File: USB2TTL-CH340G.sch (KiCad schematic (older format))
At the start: 20 parts, among them P1 PWR, P2 USB_OTG, P3 PWR_SEL, P4 CONN_01X06, U1 CH340G, X1 CRYSTAL_SMD

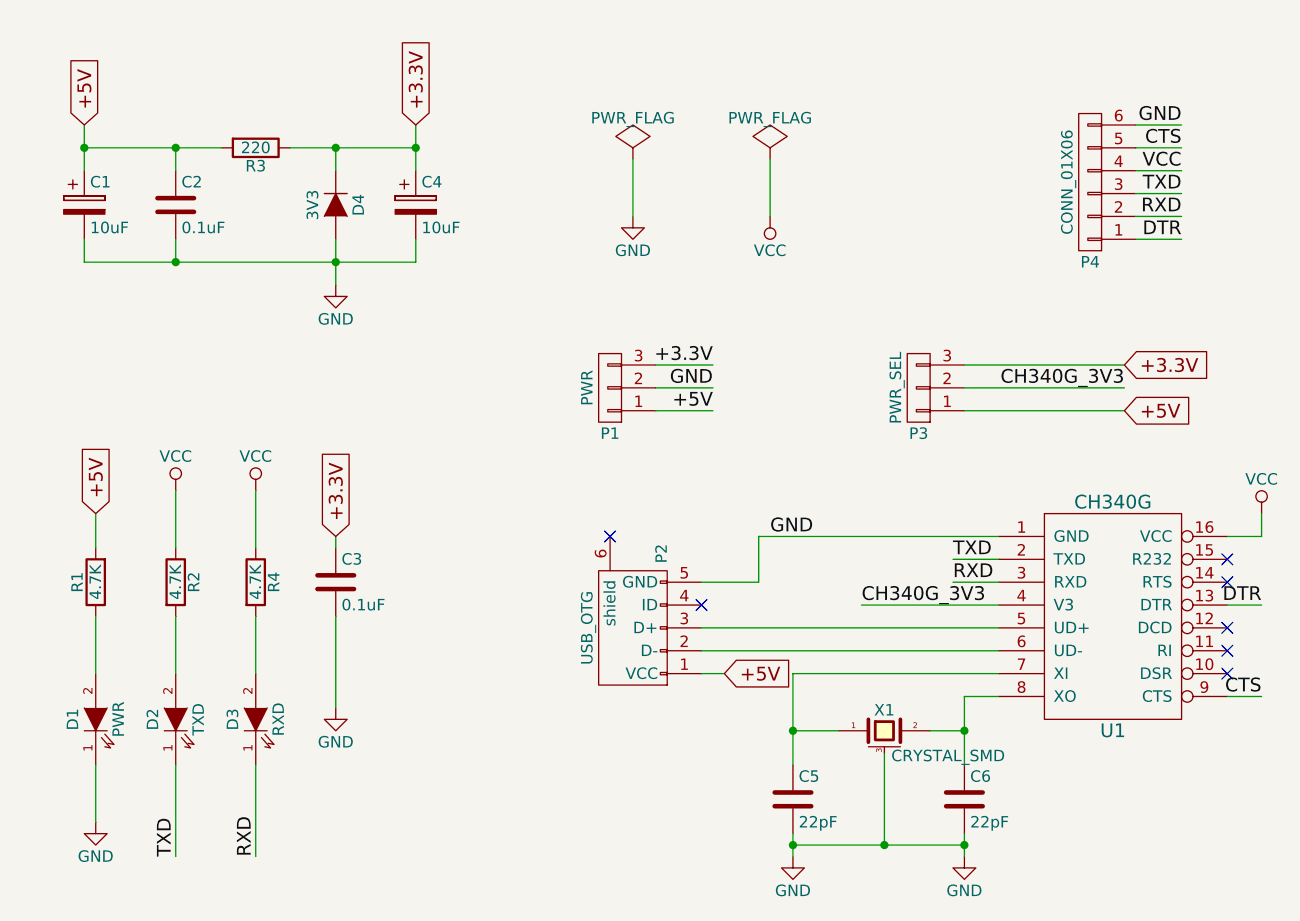
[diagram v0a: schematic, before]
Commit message: 更新为版本v0.2，修改内容如下：1.修复电源电路连接问题（v3和VCC）。2.重新布局使元件更紧凑，板型加入圆角。3.更改USB接口的封装。4.导出最新gerber及drill钻孔文件。
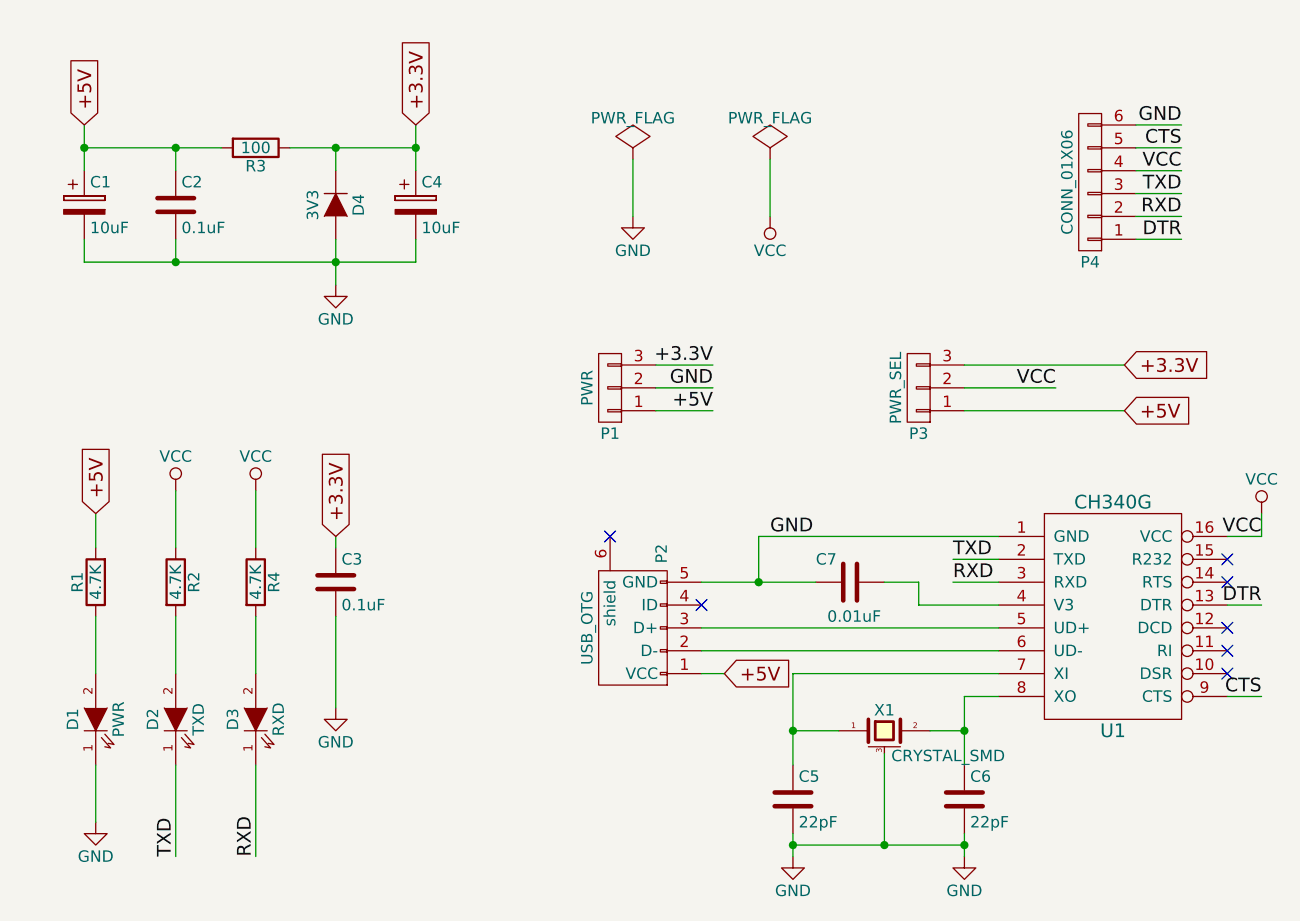
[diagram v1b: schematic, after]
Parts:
- added C7: 0.01uF, Capacitors_SMD:C_0603, symbol C
- C1, C2, C3, C4, C5, C6: footprint Capacitors_SMD:C_0603_HandSoldering -> Capacitors_SMD:C_0603
- P2: footprint Connect:USB_Micro-B -> myFootprints:USB_Micro-B-MK5
- R3: value 220 -> 100
- X1: footprint Crystals:Resonator_3.2x1.5mm -> myFootprints:Resonator_3.2x1.5mm
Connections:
- net GND: now also C7.2
- net VCC: now also P3.2 (P2)
- net CH340G_3V3: no longer names the net of U1.4 (V3)
- net CH340G_3V3: now also C7.1; no longer P3.2 (P2)
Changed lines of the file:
@@
 LIBS:valves
 LIBS:ch340g
+LIBS:USB2TTL-CH340G-cache
 EELAYER 25 0
 EELAYER END
@@
 Title "USB2TTL-CH340G"
 Date "2016-06-03"
-Rev "v0.1"
-Comp ""
-Comment1 ""
+Rev "v0.2"
+Comp "SMSLIT"
+Comment1 "Author: 5km"
 Comment2 ""
 Comment3 ""
@@
 F 0 "C1" H 3325 2950 50  0000 L CNN
 F 1 "10uF" H 3325 2750 50  0000 L CNN
-F 2 "Capacitors_SMD:C_0603_HandSoldering" H 3338 2700 50  0001 C CNN
+F 2 "Capacitors_SMD:C_0603" H 3338 2700 50  0001 C CNN
 F 3 "" H 3300 2850 50  0000 C CNN
 	1    3300 2850
@@
 F 0 "C4" H 4775 2950 50  0000 L CNN
 F 1 "10uF" H 4775 2750 50  0000 L CNN
-F 2 "Capacitors_SMD:C_0603_HandSoldering" H 4788 2700 50  0001 C CNN
+F 2 "Capacitors_SMD:C_0603" H 4788 2700 50  0001 C CNN
 F 3 "" H 4750 2850 50  0000 C CNN
 	1    4750 2850
@@
 F 0 "C2" H 3725 2950 50  0000 L CNN
 F 1 "0.1uF" H 3725 2750 50  0000 L CNN
-F 2 "Capacitors_SMD:C_0603_HandSoldering" H 3738 2700 50  0001 C CNN
+F 2 "Capacitors_SMD:C_0603" H 3738 2700 50  0001 C CNN
 F 3 "" H 3700 2850 50  0000 C CNN
 	1    3700 2850
@@
 P 4050 2600
 F 0 "R3" V 4130 2600 50  0000 C CNN
-F 1 "220" V 4050 2600 50  0000 C CNN
+F 1 "100" V 4050 2600 50  0000 C CNN
 F 2 "Resistors_SMD:R_0603" V 3980 2600 50  0001 C CNN
 F 3 "" H 4050 2600 50  0000 C CNN
@@
 F 0 "C3" H 4425 4600 50  0000 L CNN
 F 1 "0.1uF" H 4425 4400 50  0000 L CNN
-F 2 "Capacitors_SMD:C_0603_HandSoldering" H 4438 4350 50  0001 C CNN
+F 2 "Capacitors_SMD:C_0603" H 4438 4350 50  0001 C CNN
 F 3 "" H 4400 4500 50  0000 C CNN
 	1    4400 4500
@@
 F 0 "C5" H 6425 5550 50  0000 L CNN
 F 1 "22pF" H 6425 5350 50  0000 L CNN
-F 2 "Capacitors_SMD:C_0603_HandSoldering" H 6438 5300 50  0001 C CNN
+F 2 "Capacitors_SMD:C_0603" H 6438 5300 50  0001 C CNN
 F 3 "" H 6400 5450 50  0000 C CNN
 	1    6400 5450
@@
 F 0 "C6" H 7175 5550 50  0000 L CNN
 F 1 "22pF" H 7175 5350 50  0000 L CNN
-F 2 "Capacitors_SMD:C_0603_HandSoldering" H 7188 5300 50  0001 C CNN
+F 2 "Capacitors_SMD:C_0603" H 7188 5300 50  0001 C CNN
 F 3 "" H 7150 5450 50  0000 C CNN
 	1    7150 5450
@@
 NoConn ~ 8300 4800
 NoConn ~ 8300 4900
-Text Label 6700 4600 0    60   ~ 0
-CH340G_3V3
 Text Label 7100 4500 0    60   ~ 0
 RXD
@@
 	-1   0    0    1
 $EndComp
-Text Label 7850 3650 2    60   ~ 0
-CH340G_3V3
 $Comp
 L CRYSTAL_SMD X1
@@
 F 0 "X1" H 6800 5240 50  0000 C CNN
 F 1 "CRYSTAL_SMD" H 6830 5040 50  0000 L CNN
-F 2 "Crystals:Resonator_3.2x1.5mm" H 6800 5150 50  0001 C CNN
+F 2 "myFootprints:Resonator_3.2x1.5mm" H 6800 5150 50  0001 C CNN
 F 3 "" H 6800 5150 50  0000 C CNN
 	1    6800 5150
@@
 F 0 "P2" H 6025 4575 50  0000 C CNN
 F 1 "USB_OTG" H 5700 4900 50  0000 C CNN
-F 2 "Connect:USB_Micro-B" V 5650 4600 50  0001 C CNN
+F 2 "myFootprints:USB_Micro-B-MK5" V 5650 4600 50  0001 C CNN
 F 3 "" V 5650 4600 50  0000 C CNN
 	1    5700 4700
@@
 	6000 4700 7300 4700
 Wire Wire Line
-	6700 4600 7300 4600
-Wire Wire Line
 	7300 4500 7100 4500
 Wire Wire Line
@@
 Wire Wire Line
 	5700 2650 5700 2900
-Wire Wire Line
-	7150 3650 7850 3650
 Wire Wire Line
 	6400 5150 6600 5150
@@
 	6250 4500 6250 4300
 Wire Wire Line
-	6000 4500 6250 4500
+	6000 4500 6500 4500
 Text GLabel 3300 2500 1    60   Input ~ 0
 +5V
@@
 Text GLabel 3350 4200 1    60   Input ~ 0
 +5V
+Wire Wire Line
+	6950 4600 7300 4600
+$Comp
+L C C7
+U 1 1 575D2FE6
+P 6650 4500
+F 0 "C7" V 6550 4350 50  0000 L CNN
+F 1 "0.01uF" V 6800 4400 50  0000 L CNN
+F 2 "Capacitors_SMD:C_0603" H 6688 4350 50  0001 C CNN
+F 3 "" H 6650 4500 50  0000 C CNN
+	1    6650 4500
+	0    1    1    0
+$EndComp
+Wire Wire Line
+	6950 4600 6950 4500
+Wire Wire Line
+	6950 4500 6800 4500
+Connection ~ 6250 4500
+Wire Wire Line
+	7150 3650 7550 3650
+Text Label 7550 3650 2    60   ~ 0
+VCC
+Text Label 8450 4300 2    60   ~ 0
+VCC
 $EndSCHEMATC

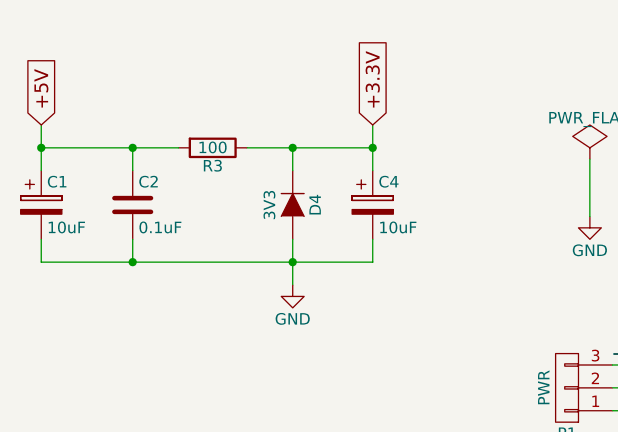
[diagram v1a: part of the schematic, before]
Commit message: 1.README中加入驱动链接及注意事项；2.更改R3电阻阻值为200欧姆；3.修改gitignore文件忽略bak文件。
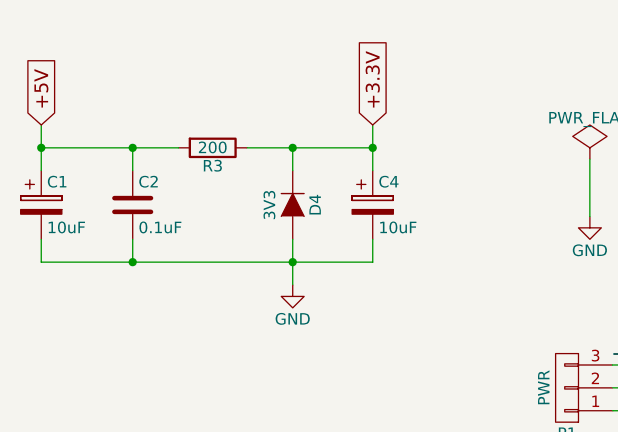
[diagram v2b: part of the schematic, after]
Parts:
- R3: value 100 -> 200
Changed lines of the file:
@@
 P 4050 2600
 F 0 "R3" V 4130 2600 50  0000 C CNN
-F 1 "100" V 4050 2600 50  0000 C CNN
+F 1 "200" V 4050 2600 50  0000 C CNN
 F 2 "Resistors_SMD:R_0603" V 3980 2600 50  0001 C CNN
 F 3 "" H 4050 2600 50  0000 C CNN

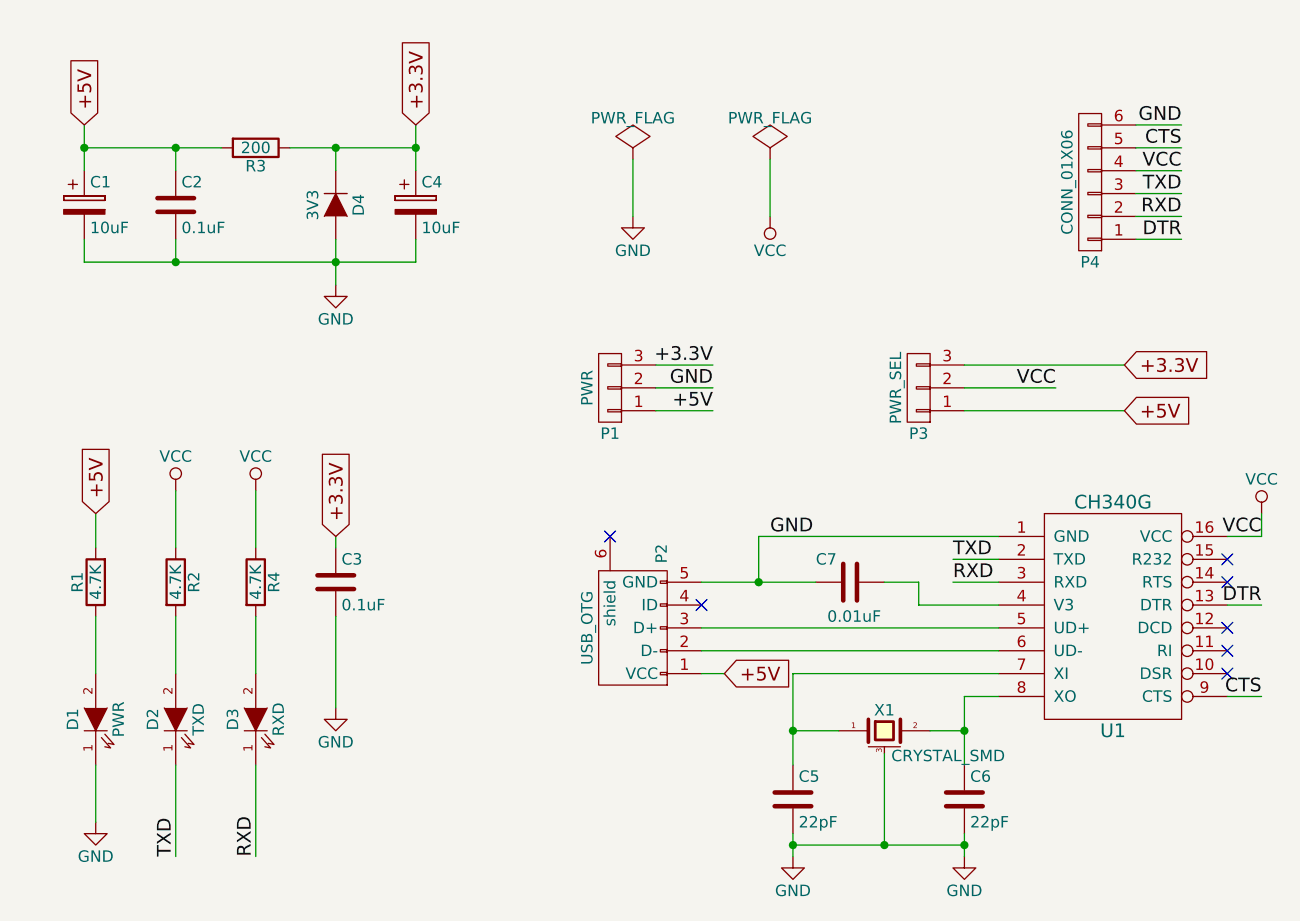
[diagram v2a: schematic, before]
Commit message: 删掉对外供电的插针，重新布局设计PCB，大小为25mmX18mm，并导出单板的gerber文件和钻孔文件
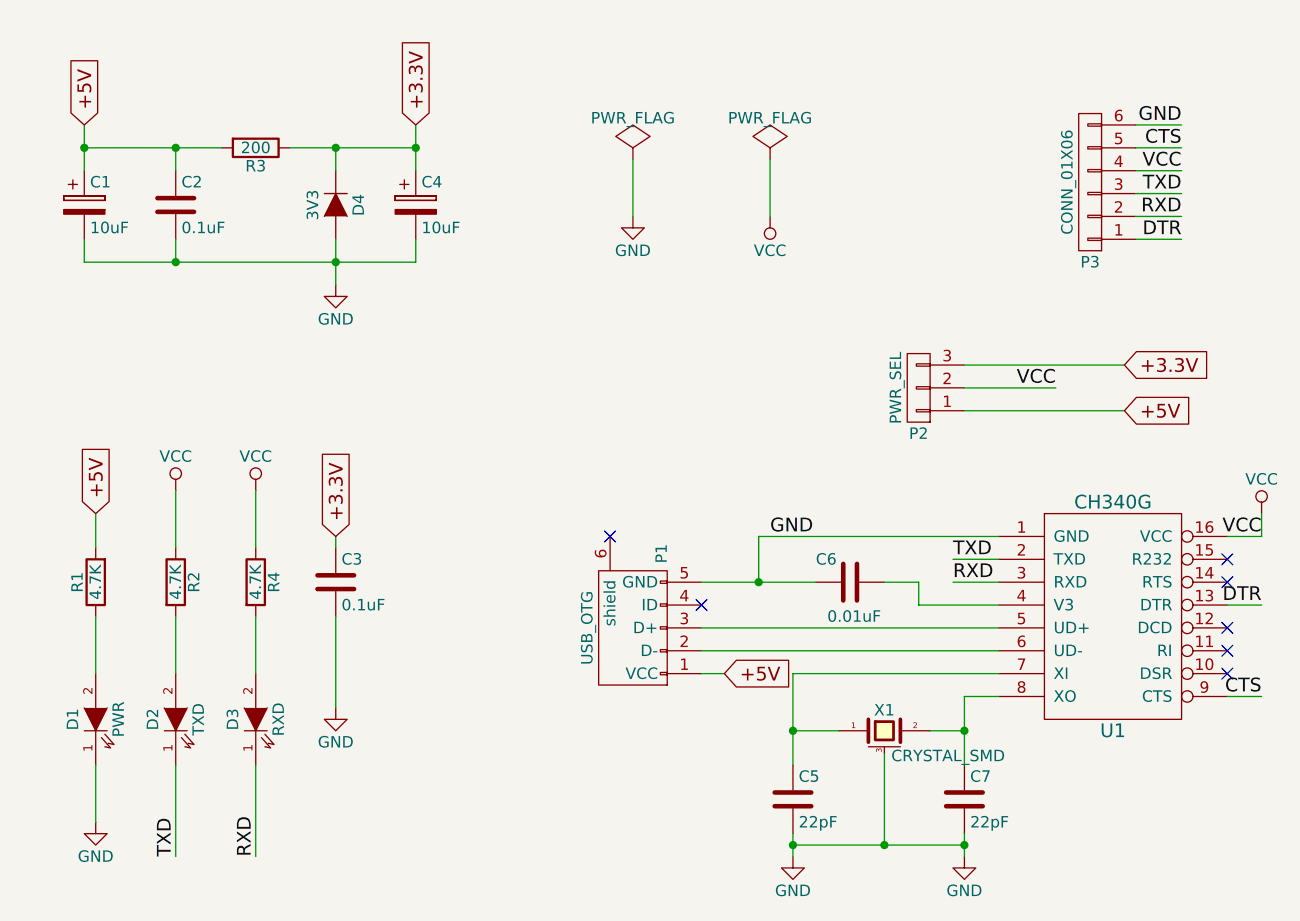
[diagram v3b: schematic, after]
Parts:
- removed P1: PWR, Pin_Headers:Pin_Header_Straight_1x03, symbol CONN_01X03
- renumbered C7 to C6, C6 to C7, P2 to P1, P3 to P2, P4 to P3
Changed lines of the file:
@@
 $EndDescr
 $Comp
-L CONN_01X06 P4
+L CONN_01X06 P3
 U 1 1 57500C21
 P 7700 2750
-F 0 "P4" H 7700 3100 50  0000 C CNN
+F 0 "P3" H 7700 3100 50  0000 C CNN
 F 1 "CONN_01X06" V 7800 2750 50  0000 C CNN
 F 2 "Pin_Headers:Pin_Header_Straight_1x06" H 7700 2750 50  0001 C CNN
@@
 $EndComp
 $Comp
-L GND #PWR01
+L GND #PWR1
 U 1 1 5750100D
 P 3350 5550
-F 0 "#PWR01" H 3350 5300 50  0001 C CNN
+F 0 "#PWR1" H 3350 5300 50  0001 C CNN
 F 1 "GND" H 3350 5400 50  0000 C CNN
 F 2 "" H 3350 5550 50  0000 C CNN
@@
 $EndComp
 $Comp
-L GND #PWR02
+L GND #PWR5
 U 1 1 5750103D
 P 4400 5050
-F 0 "#PWR02" H 4400 4800 50  0001 C CNN
+F 0 "#PWR5" H 4400 4800 50  0001 C CNN
 F 1 "GND" H 4400 4900 50  0000 C CNN
 F 2 "" H 4400 5050 50  0000 C CNN
@@
 $EndComp
 $Comp
-L GND #PWR03
+L GND #PWR8
 U 1 1 57501066
 P 6400 5700
-F 0 "#PWR03" H 6400 5450 50  0001 C CNN
+F 0 "#PWR8" H 6400 5450 50  0001 C CNN
 F 1 "GND" H 6400 5550 50  0000 C CNN
 F 2 "" H 6400 5700 50  0000 C CNN
@@
 $EndComp
 $Comp
-L GND #PWR04
+L GND #PWR9
 U 1 1 575010D5
 P 7150 5700
-F 0 "#PWR04" H 7150 5450 50  0001 C CNN
+F 0 "#PWR9" H 7150 5450 50  0001 C CNN
 F 1 "GND" H 7150 5550 50  0000 C CNN
 F 2 "" H 7150 5700 50  0000 C CNN
@@
 $EndComp
 $Comp
-L C C6
+L C C7
 U 1 1 57501276
 P 7150 5450
-F 0 "C6" H 7175 5550 50  0000 L CNN
+F 0 "C7" H 7175 5550 50  0000 L CNN
 F 1 "22pF" H 7175 5350 50  0000 L CNN
 F 2 "Capacitors_SMD:C_0603" H 7188 5300 50  0001 C CNN
@@
 $EndComp
 $Comp
-L GND #PWR05
+L GND #PWR4
 U 1 1 5750155B
 P 4400 3200
-F 0 "#PWR05" H 4400 2950 50  0001 C CNN
+F 0 "#PWR4" H 4400 2950 50  0001 C CNN
 F 1 "GND" H 4400 3050 50  0000 C CNN
 F 2 "" H 4400 3200 50  0000 C CNN
@@
 $EndComp
 $Comp
-L VCC #PWR06
+L VCC #PWR2
 U 1 1 5750585A
 P 3700 4100
-F 0 "#PWR06" H 3700 3950 50  0001 C CNN
+F 0 "#PWR2" H 3700 3950 50  0001 C CNN
 F 1 "VCC" H 3700 4250 50  0000 C CNN
 F 2 "" H 3700 4100 50  0000 C CNN
@@
 $EndComp
 $Comp
-L VCC #PWR07
+L VCC #PWR3
 U 1 1 575058E8
 P 4050 4100
-F 0 "#PWR07" H 4050 3950 50  0001 C CNN
+F 0 "#PWR3" H 4050 3950 50  0001 C CNN
 F 1 "VCC" H 4050 4250 50  0000 C CNN
 F 2 "" H 4050 4100 50  0000 C CNN
@@
 RXD
 $Comp
-L VCC #PWR08
+L VCC #PWR10
 U 1 1 575060EC
 P 8450 4200
-F 0 "#PWR08" H 8450 4050 50  0001 C CNN
+F 0 "#PWR10" H 8450 4050 50  0001 C CNN
 F 1 "VCC" H 8450 4350 50  0000 C CNN
 F 2 "" H 8450 4200 50  0000 C CNN
@@
 DTR
 $Comp
-L CONN_01X03 P1
-U 1 1 57507C87
-P 5600 3650
-F 0 "P1" H 5600 3850 50  0000 C CNN
-F 1 "PWR" V 5700 3650 50  0000 C CNN
-F 2 "Pin_Headers:Pin_Header_Straight_1x03" H 5600 3650 50  0001 C CNN
-F 3 "" H 5600 3650 50  0000 C CNN
-	1    5600 3650
-	-1   0    0    1
-$EndComp
-Text Label 6050 3550 2    60   ~ 0
-+3.3V
-Text Label 6050 3650 2    60   ~ 0
-GND
-Text Label 6050 3750 2    60   ~ 0
-+5V
-$Comp
-L PWR_FLAG #FLG09
+L PWR_FLAG #FLG2
 U 1 1 57508993
 P 6300 2650
-F 0 "#FLG09" H 6300 2745 50  0001 C CNN
+F 0 "#FLG2" H 6300 2745 50  0001 C CNN
 F 1 "PWR_FLAG" H 6300 2830 50  0000 C CNN
 F 2 "" H 6300 2650 50  0000 C CNN
@@
 $EndComp
 $Comp
-L VCC #PWR010
+L VCC #PWR7
 U 1 1 57508B09
 P 6300 2900
-F 0 "#PWR010" H 6300 2750 50  0001 C CNN
+F 0 "#PWR7" H 6300 2750 50  0001 C CNN
 F 1 "VCC" H 6300 3050 50  0000 C CNN
 F 2 "" H 6300 2900 50  0000 C CNN
@@
 NoConn ~ 5600 4300
 $Comp
-L PWR_FLAG #FLG011
+L PWR_FLAG #FLG1
 U 1 1 5750AEC9
 P 5700 2650
-F 0 "#FLG011" H 5700 2745 50  0001 C CNN
+F 0 "#FLG1" H 5700 2745 50  0001 C CNN
 F 1 "PWR_FLAG" H 5700 2830 50  0000 C CNN
 F 2 "" H 5700 2650 50  0000 C CNN
@@
 $EndComp
 $Comp
-L GND #PWR012
+L GND #PWR6
 U 1 1 5750AF10
 P 5700 2900
-F 0 "#PWR012" H 5700 2650 50  0001 C CNN
+F 0 "#PWR6" H 5700 2650 50  0001 C CNN
 F 1 "GND" H 5700 2750 50  0000 C CNN
 F 2 "" H 5700 2900 50  0000 C CNN
@@
 $EndComp
 $Comp
-L CONN_01X03 P3
+L CONN_01X03 P2
 U 1 1 5750B4CF
 P 6950 3650
-F 0 "P3" H 6950 3850 50  0000 C CNN
+F 0 "P2" H 6950 3850 50  0000 C CNN
 F 1 "PWR_SEL" V 7050 3650 50  0000 C CNN
 F 2 "Pin_Headers:Pin_Header_Straight_1x03" H 6950 3650 50  0001 C CNN
@@
 $EndComp
 $Comp
-L USB_OTG P2
+L USB_OTG P1
 U 1 1 5750F0F3
 P 5700 4700
-F 0 "P2" H 6025 4575 50  0000 C CNN
+F 0 "P1" H 6025 4575 50  0000 C CNN
 F 1 "USB_OTG" H 5700 4900 50  0000 C CNN
 F 2 "myFootprints:USB_Micro-B-MK5" V 5650 4600 50  0001 C CNN
@@
 Wire Wire Line
 	8300 5000 8450 5000
-Wire Wire Line
-	5800 3550 6050 3550
-Wire Wire Line
-	5800 3650 6050 3650
-Wire Wire Line
-	5800 3750 6050 3750
 Wire Wire Line
 	6300 2650 6300 2900
@@
 	6950 4600 7300 4600
 $Comp
-L C C7
+L C C6
 U 1 1 575D2FE6
 P 6650 4500
-F 0 "C7" V 6550 4350 50  0000 L CNN
+F 0 "C6" V 6550 4350 50  0000 L CNN
 F 1 "0.01uF" V 6800 4400 50  0000 L CNN
 F 2 "Capacitors_SMD:C_0603" H 6688 4350 50  0001 C CNN
